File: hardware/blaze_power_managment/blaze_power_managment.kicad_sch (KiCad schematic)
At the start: 62 parts, among them J1 Conn_01x30_Pin, J2 Conn_01x30_Socket, J3 XT30, J4 XT30, J5 JTAG, Q1 DMG2305, SW1 SW_SPST, SW2 SW_SPDT, U1 TCAN1044VDDFR, U2 TPS62913, U3 INA2181, U4 TPS62913, U5 STM32H503KBUx

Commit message: Completed initial routing
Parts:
- removed J1: Conn_01x30_Pin, Blaze_Library:HRS_DF17_1.0H_-30DP-0.5V_57_, symbol Connector:Conn_01x30_Pin
- removed J2: Conn_01x30_Socket, Blaze_Library:HRS_DF17_1.0H_-30DP-0.5V_57_, symbol Connector:Conn_01x30_Socket
- added J1: FrontInterconnect, Blaze_Library:HRS_DF17_1.0H_-30DP-0.5V_57_, symbol Blaze_Lib:DF17U-30_Male
- added J2: RearInterconnect, Blaze_Library:HRS_DF17_1.0H_-30DP-0.5V_57_, symbol Blaze_Lib:DF17U-30_Female
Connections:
- net +3V3: now also J1.10 (Pin_10), J1.16 (Pin_16), J1.27 (Pin_27), J1.28 (Pin_28), J2.15 (Pin_15), J2.21 (Pin_21), J2.3 (Pin_3), J2.4 (Pin_4)
- net +5V: now also J1.25 (Pin_25), J1.26 (Pin_26), J1.9 (Pin_9), J2.22 (Pin_22), J2.5 (Pin_5), J2.6 (Pin_6)
- net 3V3_SENSE: now also U5.6 (PA0); no longer C15.1, C16.1, C17.1, L2.2, R10.1, R11.1, R12.2, R13.1, U4.3 (VO), U5.7 (PA1)
- net 3V3_SENSE_IN: now also C15.1, C16.1, C17.1, L2.2, R10.1, R11.1, R12.2, R13.1, U4.3 (VO)
- net 5V_SENSE: now also U5.7 (PA1); no longer C7.1, C8.1, C9.1, L1.2, R4.1, R5.1, R6.2, R7.1, U2.3 (VO), U5.6 (PA0)
- net 5V_SENSE_IN: now also C7.1, C8.1, C9.1, L1.2, R4.1, R5.1, R6.2, R7.1, U2.3 (VO)
- net ARM: now also J1.6 (Pin_6), J2.25 (Pin_25)
- net CANH: now also J1.21 (Pin_21), J2.10 (Pin_10)
- net CANL: now also J1.22 (Pin_22), J2.9 (Pin_9)
- net GND: now also J3.1 (Pin_1), J1.1 (Pin_1), J1.12 (Pin_12), J1.13 (Pin_13), J1.19 (Pin_19), J1.2 (Pin_2), J1.20 (Pin_20), J1.S1 (Tab_1), J1.S2 (Tab_2), J2.11 (Pin_11), J2.12 (Pin_12), J2.18 (Pin_18), J2.19 (Pin_19), J2.29 (Pin_29), J2.30 (Pin_30), J2.S1 (Tab_1), J2.S2 (Tab_2); no longer J4.2 (Pin_2)
- net PPS: now also J1.11 (Pin_11), J2.20 (Pin_20)
- net at Q1.1 (D): now also J4.2 (Pin_2); no longer J3.1 (Pin_1)
- new net: J1.30 (Pin_30), J2.1 (Pin_1)
- new net: J1.18 (Pin_18), J2.13 (Pin_13)
- new net: J1.17 (Pin_17), J2.14 (Pin_14)
- new net: J1.15 (Pin_15), J2.16 (Pin_16)
- new net: J1.14 (Pin_14), J2.17 (Pin_17)
- new net: J1.29 (Pin_29), J2.2 (Pin_2)
- new net: J1.8 (Pin_8), J2.23 (Pin_23)
- new net: J1.7 (Pin_7), J2.24 (Pin_24)
- new net: J1.5 (Pin_5), J2.26 (Pin_26)
- new net: J1.24 (Pin_24), J2.7 (Pin_7)
- new net: J1.23 (Pin_23), J2.8 (Pin_8)
- new net RX_RADIO: J1.4 (Pin_4), J2.27 (Pin_27)
- new net TX_RADIO: J1.3 (Pin_3), J2.28 (Pin_28)

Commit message: power routing
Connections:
- net CANH: now also D1.1 (K1); no longer D1.2 (K2)
- net CANL: now also D1.2 (K2); no longer D1.1 (K1)

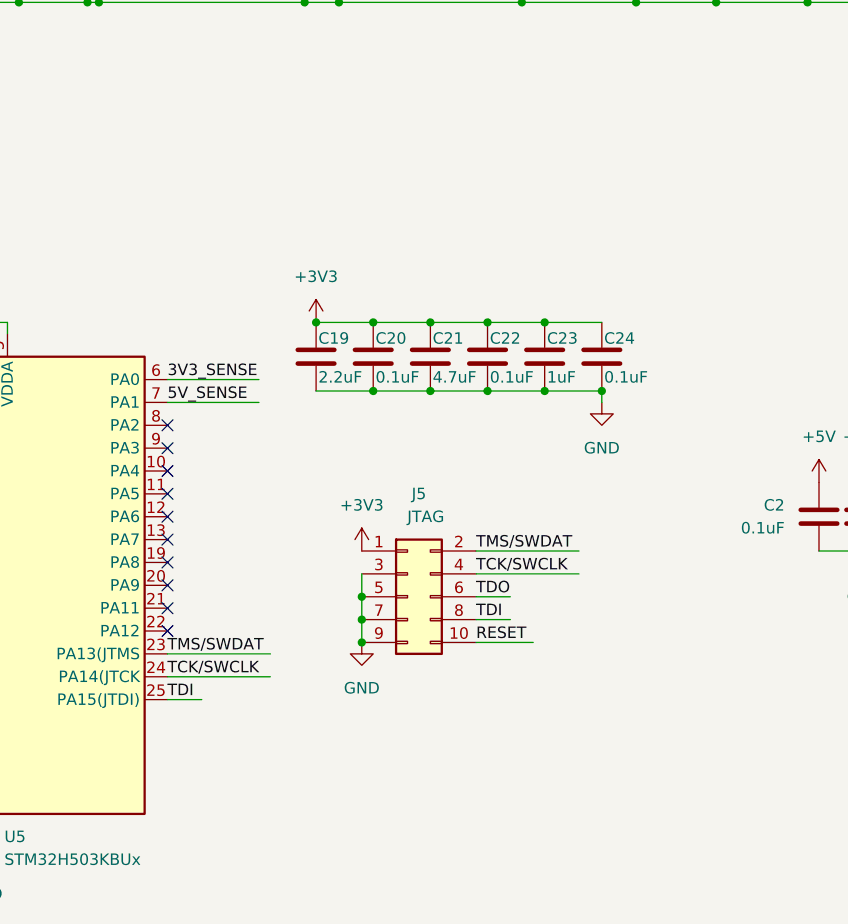
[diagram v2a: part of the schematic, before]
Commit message: Added voltage sensing
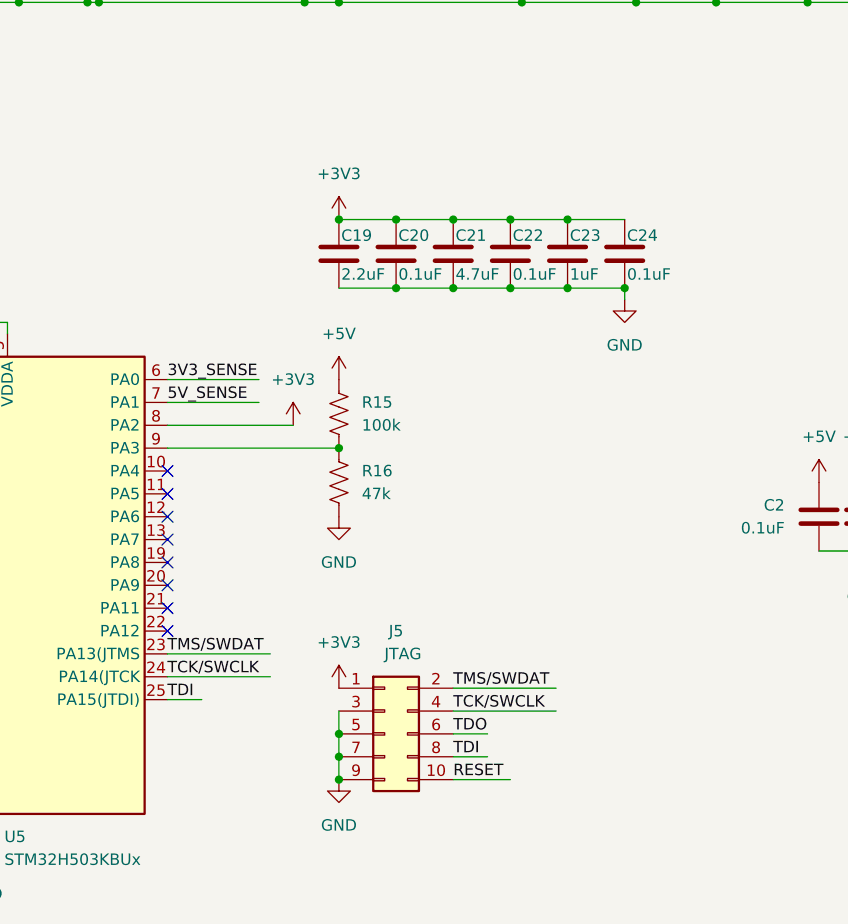
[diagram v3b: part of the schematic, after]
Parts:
- added R15: 100k, Resistor_SMD:R_0603_1608Metric, symbol Device:R_US
- added R16: 47k, Resistor_SMD:R_0603_1608Metric, symbol Device:R_US
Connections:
- net +3V3: now also U5.8 (PA2)
- net +5V: now also R15.1
- net GND: now also R16.2
- net at U5.9 (PA3): now also R15.2, R16.1
- no-connect marks 16 -> 14
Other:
- moved on the sheet: C19, C20, C21, C22, C23, C24, J5
